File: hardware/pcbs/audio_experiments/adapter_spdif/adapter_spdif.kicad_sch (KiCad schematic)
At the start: 11 parts, among them U7 74HCU04

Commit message: finalise SPDIF adapter board
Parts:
- removed C58: 10nF, Capacitor_SMD:C_0805_2012Metric, symbol Device:C_Small
- removed C59: 150nF, Capacitor_SMD:C_0805_2012Metric, symbol Device:C_Small
- removed JP1: SPDIF_OUT_INVERT, Jumper:SolderJumper-3_P1.3mm_Bridged2Bar12_RoundedPad1.0x1.5mm, symbol Jumper:SolderJumper_3_Bridged12
- removed JP2: SPDIF_IN_INVERT, Jumper:SolderJumper-3_P1.3mm_Bridged2Bar12_RoundedPad1.0x1.5mm, symbol Jumper:SolderJumper_3_Bridged12
- removed R55: 75Ω, Resistor_SMD:R_0805_2012Metric, symbol Device:R
- removed R56, R57: 10kΩ, Resistor_SMD:R_0805_2012Metric, symbol Device:R
- removed R58: 200Ω, Resistor_SMD:R_0805_2012Metric, symbol Device:R
- removed R59: 93Ω, Resistor_SMD:R_0805_2012Metric, symbol Device:R
- removed unit 2 of U7
- removed unit 4 of U7
- removed unit 1 of U7
- removed unit 5 of U7
- removed unit 6 of U7
- removed unit 3 of U7
- added H1, H3: MountingHole_Pad, MountingHole:MountingHole_3.2mm_M3_Pad_Via, symbol Mechanical:MountingHole_Pad
- added J1: Header_Horizontal_01x04, conn:PinHeader_1x04_P2.54mm_Vertical, symbol conn:Conn_01x04
- added J2: Conn_Coaxial_2x, conn:RCJ2123, symbol conn:Conn_Coaxial_2x
- renumbered C57 to C1, U7 to U1
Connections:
- net +3.3V: now also U1.14 (VCC), J1.1 (Pin_1); no longer U1.7 (GND)
- net GND: now also U1.7 (GND), H1.1, H3.1, J1.4 (Pin_4), J2.1 (Ext), J2.3 (Ext); no longer U1.14 (VCC)
- new net SPDIF In/SPDIF_IN_LOG: J1.3 (Pin_3)
- new net SPDIF In/SPDIF_IN_RAW: J2.4 (In)
- new net SPDIF Out/SPDIF_OUT_LOG: J1.2 (Pin_2)
- new net SPDIF Out/SPDIF_OUT_RAW: J2.2 (In)
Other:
- added sheet SPDIF In (spdif_in.kicad_sch)
- added sheet SPDIF Out (spdif_out.kicad_sch)
- moved on the sheet: C1, U1G

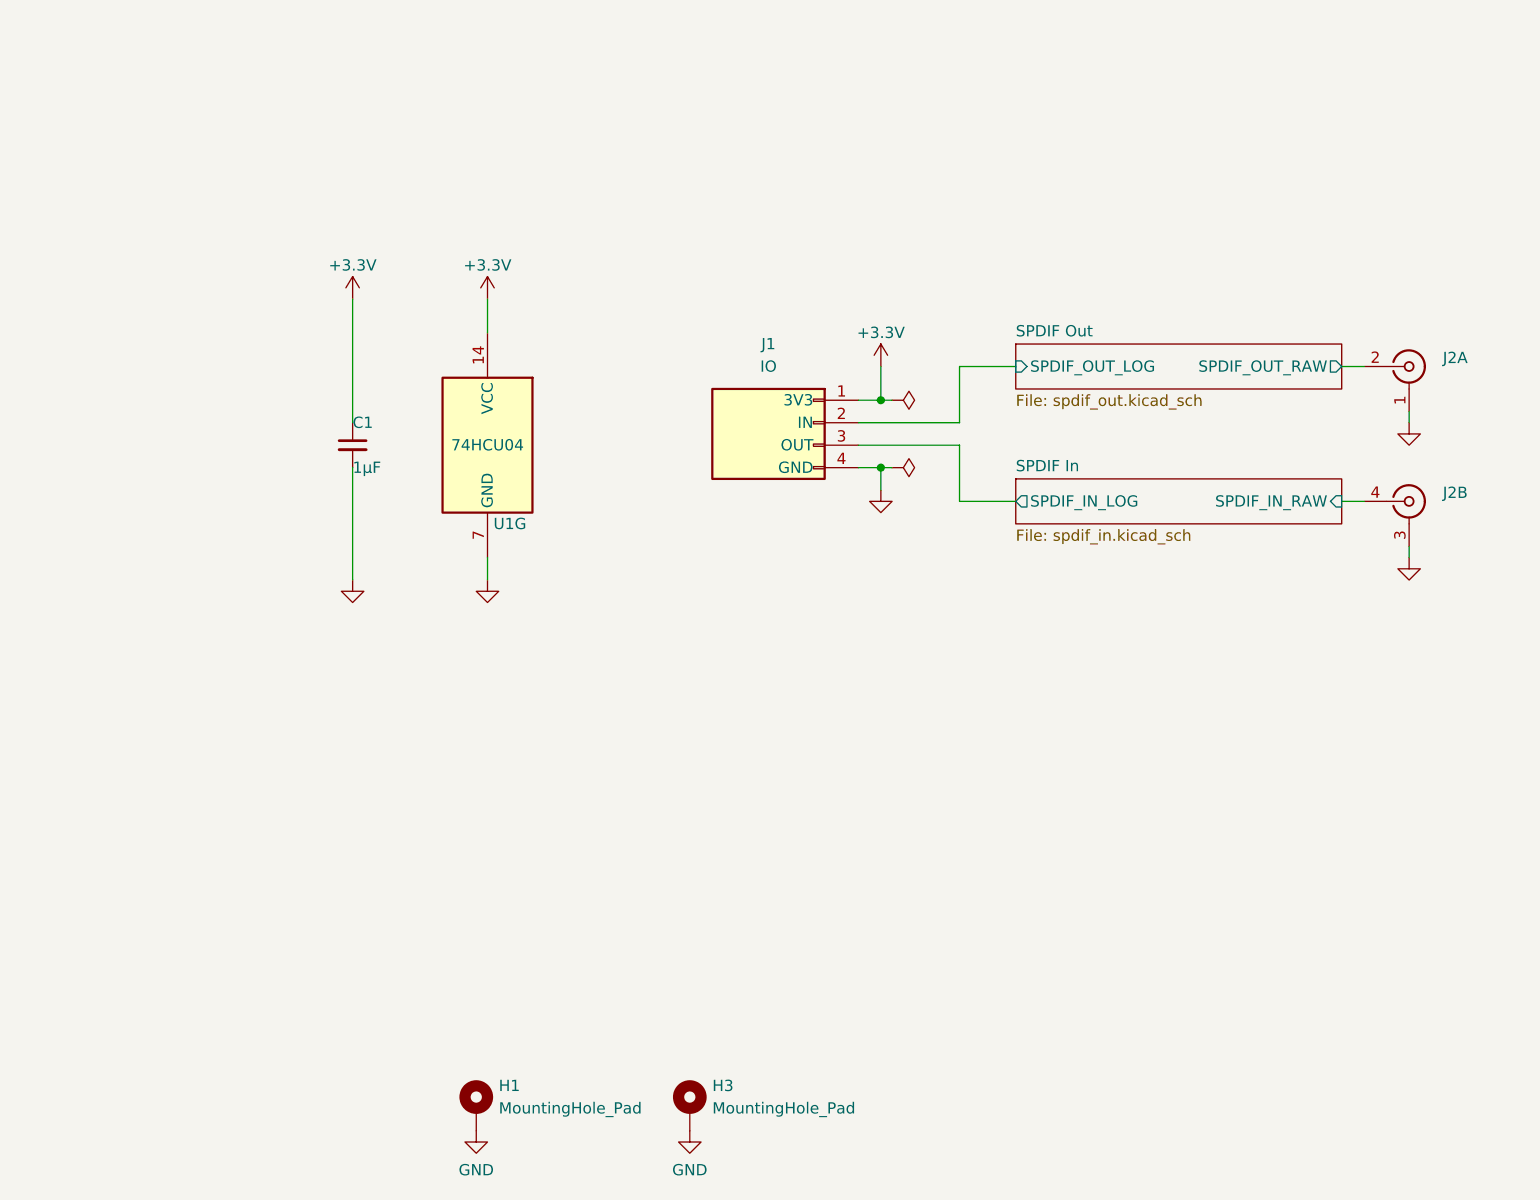
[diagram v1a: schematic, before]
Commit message: rearrange addon header
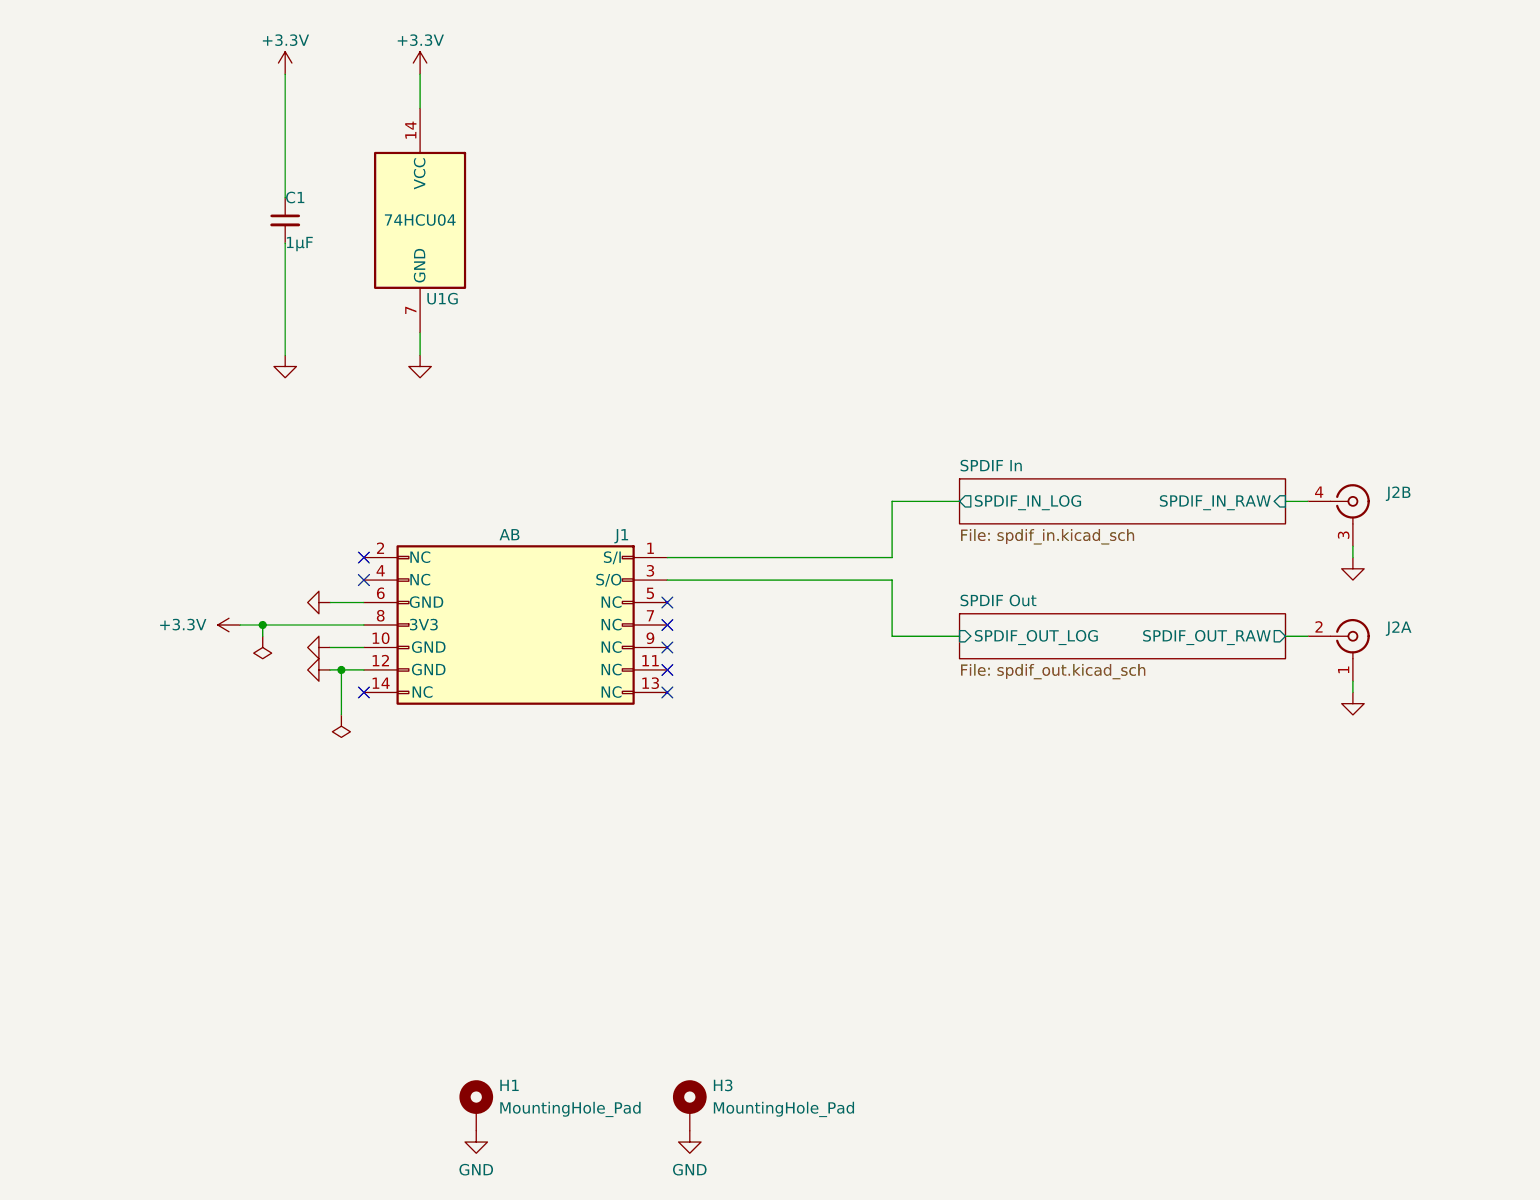
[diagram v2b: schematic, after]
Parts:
- removed J1: Header_Horizontal_01x04, conn:PinHeader_1x04_P2.54mm_Vertical, symbol conn:Conn_01x04
- added J1: Conn_02x07_Odd_Even, conn:PinHeader_2x07_P2.54mm_Vertical, symbol conn:Conn_02x07_Odd_Even
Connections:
- net +3.3V: now also J1.8 (Pin_8)
- net GND: now also J1.10 (Pin_10), J1.12 (Pin_12), J1.6 (Pin_6)
- net SPDIF In/SPDIF_IN_LOG: now also J1.1 (Pin_1)
- net SPDIF Out/SPDIF_OUT_LOG: now also J1.3 (Pin_3)
- no-connect marks 0 -> 8
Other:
- moved on the sheet: C1, J2A, J2B, U1G
